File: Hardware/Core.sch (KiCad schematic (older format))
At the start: 45 parts

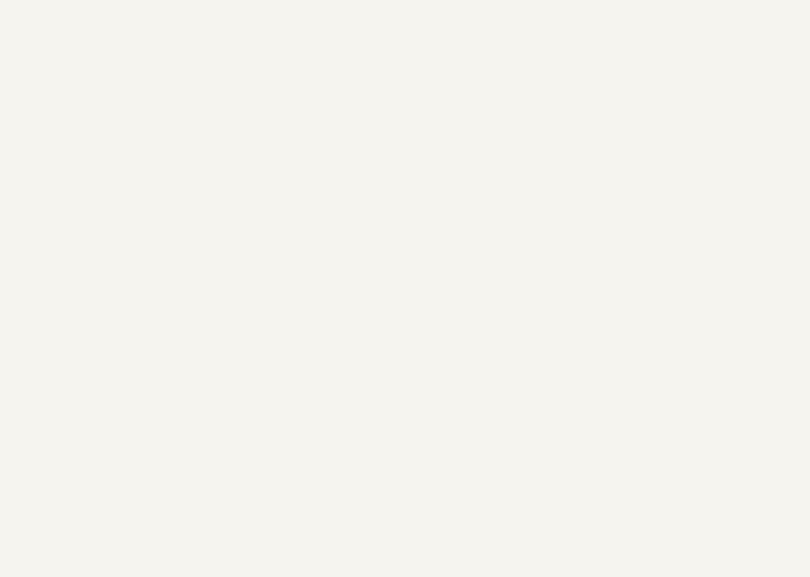
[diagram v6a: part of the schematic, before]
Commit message: Add SD card to core
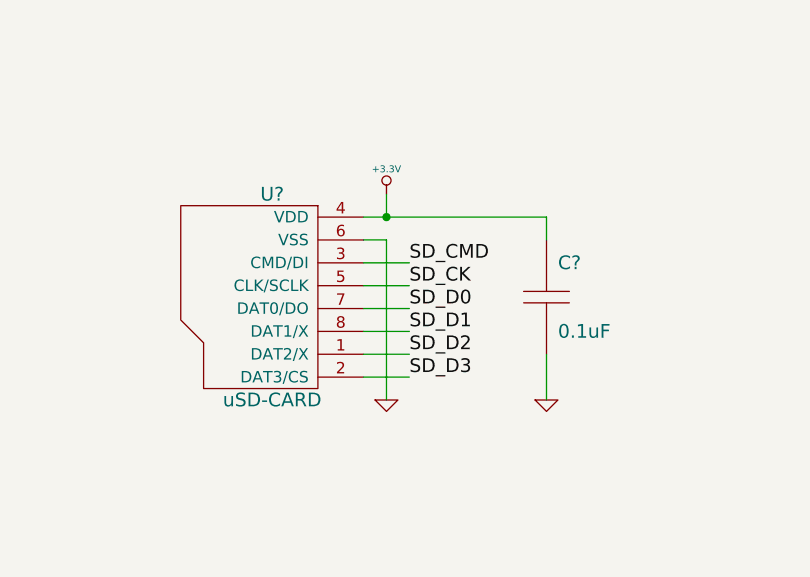
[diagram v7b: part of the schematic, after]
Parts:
- added C?: 0.1uF, CAPC1005-N, symbol C
- added U?: uSD-CARD, symbol SDCARD-FULL-MICRO
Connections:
- net +3.3V: now also C?.1, U?.4 (VDD)
- net GND: now also C?.2, U?.6 (VSS)
- net SD_CK: now also U?.5 (CLK/SCLK)
- net SD_CMD: now also U?.3 (CMD/DI)
- net SD_D0: now also U?.7 (DAT0/DO)
- net SD_D1: now also U?.8 (DAT1/X)
- net SD_D2: now also U?.1 (DAT2/X)
- net SD_D3: now also U?.2 (DAT3/CS)
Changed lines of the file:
@@
 Sheet 4 4
 Title "Hyperion"
-Date "30 apr 2014"
+Date "1 may 2014"
 Rev "0.2"
 Comp "Aerodyne Labs"
@@
 Wire Wire Line
 	6700 9100 6700 9400
+$Comp
+L SDCARD-FULL-MICRO U?
+U 1 1 5362C961
+P 2800 7650
+F 0 "U?" H 2800 8100 60  0000 C CNN
+F 1 "uSD-CARD" H 2800 7200 60  0000 C CNN
+F 2 "" H 2800 7650 60  0000 C CNN
+F 3 "" H 2800 7650 60  0000 C CNN
+	1    2800 7650
+	1    0    0    -1
+$EndComp
+$Comp
+L C C?
+U 1 1 5362C973
+P 4000 7650
+F 0 "C?" H 4050 7800 60  0000 L CNN
+F 1 "0.1uF" H 4050 7500 60  0000 L CNN
+F 2 "CAPC1005-N" H 4000 7650 60  0001 C CNN
+F 3 "~" H 4000 7650 60  0000 C CNN
+F 4 "Samsung" H 4000 7650 60  0001 C CNN "MFR Name"
+F 5 "CL05A104MP5NNNC" H 4000 7650 60  0001 C CNN "MFR Part No"
+F 6 "1276-1443-1-ND" H 4000 7650 60  0001 C CNN "Distributor Part No"
+F 7 "10V" H 3950 7500 60  0001 R CNN "Voltage"
+F 8 "X5R" H 3950 7800 60  0001 R CNN "Dielectric"
+	1    4000 7650
+	1    0    0    -1
+$EndComp
+Text Label 3400 7700 0    60   ~ 0
+SD_D0
+Text Label 3400 7800 0    60   ~ 0
+SD_D1
+Text Label 3400 7900 0    60   ~ 0
+SD_D2
+Text Label 3400 8000 0    60   ~ 0
+SD_D3
+Text Label 3400 7600 0    60   ~ 0
+SD_CK
+Text Label 3400 7500 0    60   ~ 0
+SD_CMD
+$Comp
+L GND #PWR?
+U 1 1 5362C997
+P 3300 8100
+F 0 "#PWR?" H 3300 8100 30  0001 C CNN
+F 1 "GND" H 3300 8030 30  0001 C CNN
+F 2 "" H 3300 8100 60  0000 C CNN
+F 3 "" H 3300 8100 60  0000 C CNN
+	1    3300 8100
+	1    0    0    -1
+$EndComp
+$Comp
+L +3.3V #PWR?
+U 1 1 5362C9A6
+P 3300 7200
+F 0 "#PWR?" H 3300 7160 30  0001 C CNN
+F 1 "+3.3V" H 3300 7310 30  0000 C CNN
+F 2 "" H 3300 7200 60  0000 C CNN
+F 3 "" H 3300 7200 60  0000 C CNN
+	1    3300 7200
+	1    0    0    -1
+$EndComp
+Wire Wire Line
+	3300 7200 3300 7300
+Wire Wire Line
+	3200 7300 4000 7300
+Wire Wire Line
+	3200 7400 3300 7400
+Wire Wire Line
+	3300 7400 3300 8100
+Wire Wire Line
+	3200 7500 3400 7500
+Wire Wire Line
+	3200 7600 3400 7600
+Wire Wire Line
+	3200 7700 3400 7700
+Wire Wire Line
+	3200 7800 3400 7800
+Wire Wire Line
+	3200 7900 3400 7900
+Wire Wire Line
+	3200 8000 3400 8000
+Wire Wire Line
+	4000 7300 4000 7400
+Connection ~ 3300 7300
+$Comp
+L GND #PWR?
+U 1 1 5362CF7A
+P 4000 8100
+F 0 "#PWR?" H 4000 8100 30  0001 C CNN
+F 1 "GND" H 4000 8030 30  0001 C CNN
+F 2 "" H 4000 8100 60  0000 C CNN
+F 3 "" H 4000 8100 60  0000 C CNN
+	1    4000 8100
+	1    0    0    -1
+$EndComp
+Wire Wire Line
+	4000 8100 4000 7900
 $EndSCHEMATC

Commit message: Add secondary oscillator
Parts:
- added C? (x2): C, ~, symbol C
- added X?: CRYSTAL, ~, symbol CRYSTAL
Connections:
- net GND: now also C?.2, C?.2
- net SOSC0: now also C?.1, X?.1
- net SOSC1: now also C?.1, X?.2
- net ~RST: now also U?.12 (~RST), U?.12 (~RST)
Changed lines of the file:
@@
 Sheet 4 4
 Title "Hyperion"
-Date "1 may 2014"
+Date "2 may 2014"
 Rev "0.2"
 Comp "Aerodyne Labs"
@@
 Wire Wire Line
 	4000 8100 4000 7900
+Text Label 14000 6200 0    60   ~ 0
+~RST
+Text Label 14000 3000 0    60   ~ 0
+~RST
+Wire Wire Line
+	14000 3000 13800 3000
+Wire Wire Line
+	13800 6200 14000 6200
+$Comp
+L CRYSTAL X?
+U 1 1 5362EAA5
+P 9850 9800
+F 0 "X?" H 9850 9950 60  0000 C CNN
+F 1 "CRYSTAL" H 9850 9650 60  0000 C CNN
+F 2 "~" H 9850 9800 60  0000 C CNN
+F 3 "~" H 9850 9800 60  0000 C CNN
+	1    9850 9800
+	1    0    0    -1
+$EndComp
+$Comp
+L C C?
+U 1 1 5362EAB4
+P 10200 10150
+F 0 "C?" H 10250 10300 60  0000 L CNN
+F 1 "C" H 10250 10000 60  0000 L CNN
+F 2 "~" H 10200 10150 60  0000 C CNN
+F 3 "~" H 10200 10150 60  0000 C CNN
+F 4 "V" H 10150 10000 60  0001 R CNN "Voltage"
+F 5 "D" H 10150 10300 60  0001 R CNN "Dielectric"
+	1    10200 10150
+	1    0    0    -1
+$EndComp
+$Comp
+L C C?
+U 1 1 5362EACF
+P 9500 10150
+F 0 "C?" H 9550 10300 60  0000 L CNN
+F 1 "C" H 9550 10000 60  0000 L CNN
+F 2 "~" H 9500 10150 60  0000 C CNN
+F 3 "~" H 9500 10150 60  0000 C CNN
+F 4 "V" H 9450 10000 60  0001 R CNN "Voltage"
+F 5 "D" H 9450 10300 60  0001 R CNN "Dielectric"
+	1    9500 10150
+	-1   0    0    -1
+$EndComp
+Text Label 9500 9700 1    60   ~ 0
+SOSC0
+Text Label 10200 9700 1    60   ~ 0
+SOSC1
+Wire Wire Line
+	10200 9700 10200 9900
+Wire Wire Line
+	10100 9800 10200 9800
+Connection ~ 10200 9800
+Wire Wire Line
+	9500 9700 9500 9900
+Wire Wire Line
+	9600 9800 9500 9800
+Connection ~ 9500 9800
+$Comp
+L GND #PWR?
+U 1 1 5362F0A3
+P 9500 10500
+F 0 "#PWR?" H 9500 10500 30  0001 C CNN
+F 1 "GND" H 9500 10430 30  0001 C CNN
+F 2 "" H 9500 10500 60  0000 C CNN
+F 3 "" H 9500 10500 60  0000 C CNN
+	1    9500 10500
+	1    0    0    -1
+$EndComp
+$Comp
+L GND #PWR?
+U 1 1 5362F0B2
+P 10200 10500
+F 0 "#PWR?" H 10200 10500 30  0001 C CNN
+F 1 "GND" H 10200 10430 30  0001 C CNN
+F 2 "" H 10200 10500 60  0000 C CNN
+F 3 "" H 10200 10500 60  0000 C CNN
+	1    10200 10500
+	1    0    0    -1
+$EndComp
+Wire Wire Line
+	10200 10500 10200 10400
+Wire Wire Line
+	9500 10400 9500 10500
 $EndSCHEMATC
